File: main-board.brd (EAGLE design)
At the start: 49.2 x 17.8 mm, 53 parts, among them IC1 MEGA328-PB, IC2 MCP73831, IC3 LE33, Q1 3,6864 MHz, Q4 TSM2302CX, T1 IRF7306

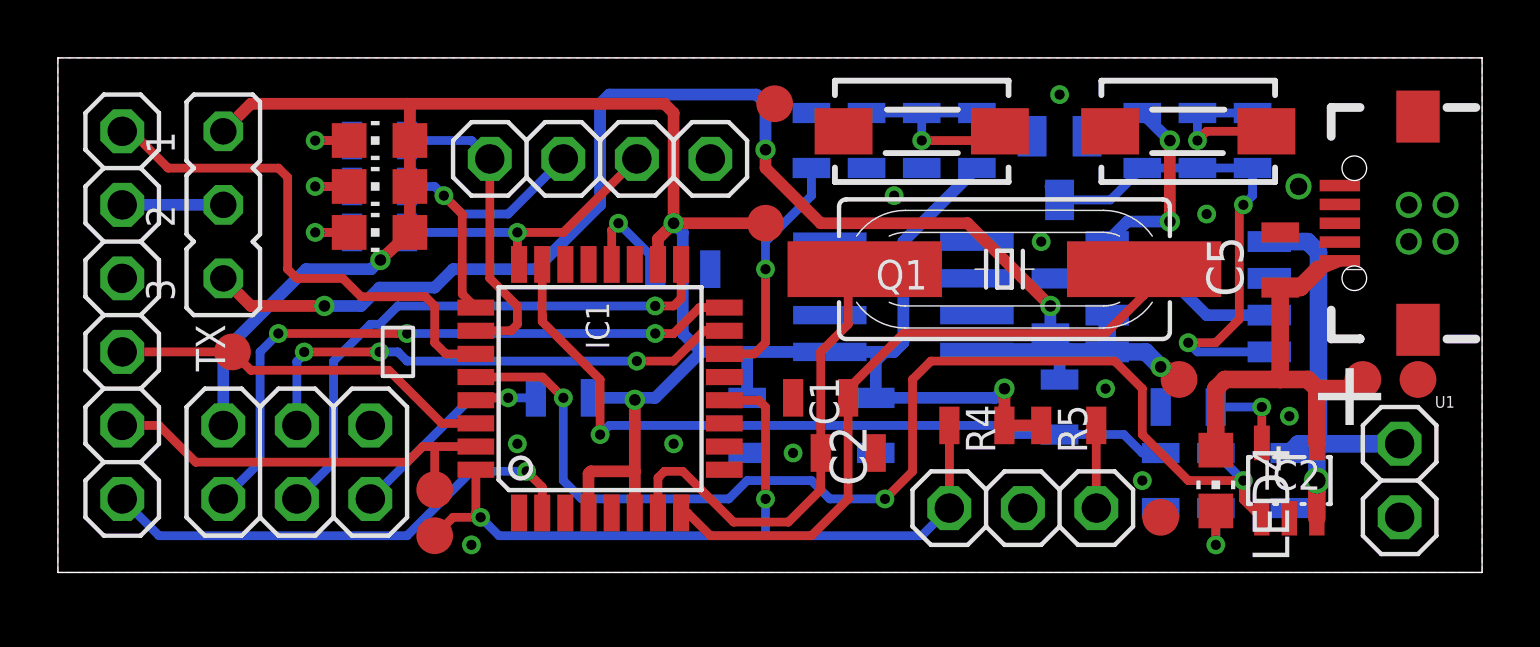
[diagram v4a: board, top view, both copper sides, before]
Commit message: Fix polarity-protection MOSFET.
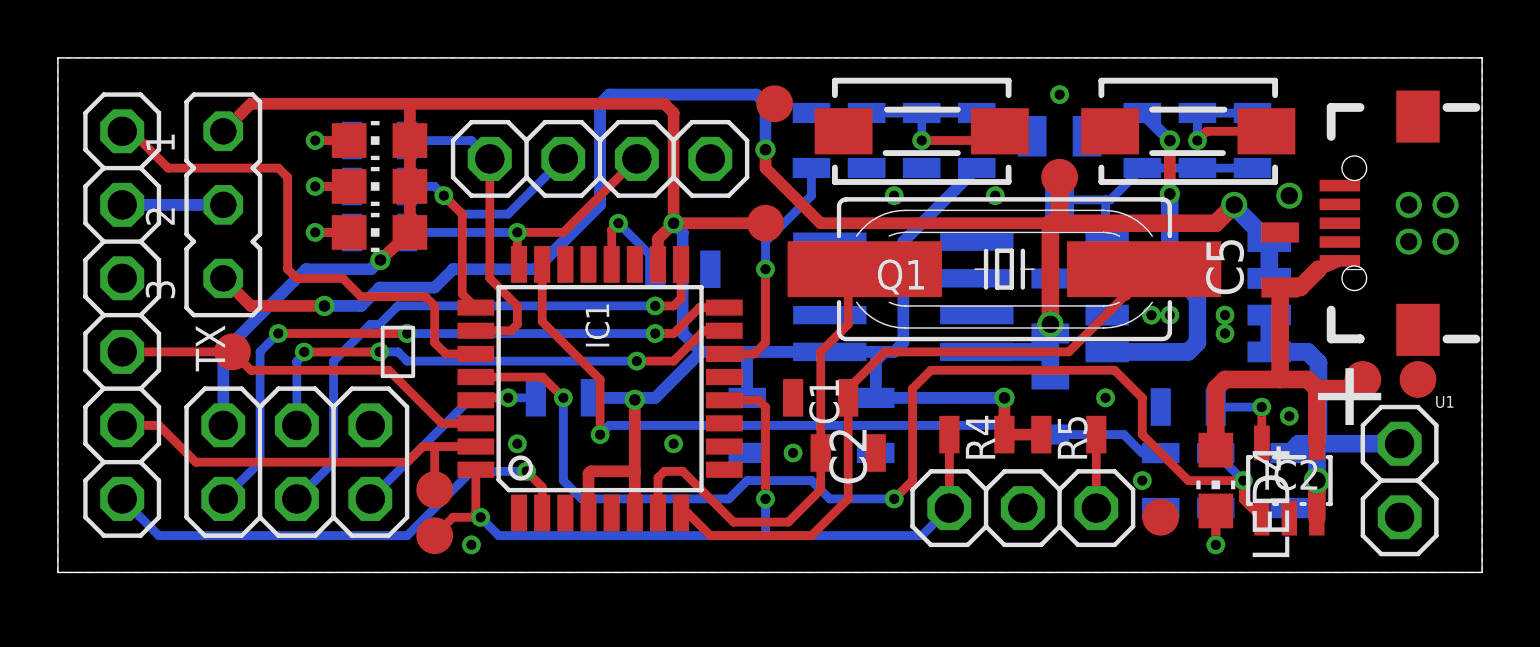
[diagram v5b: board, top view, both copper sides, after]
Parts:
- moved TP5 8.11 mm to (34.6, 13.7)
- moved R7 0.32 mm to (34.3, 5.71)
- moved R4 0.32 mm to (31.8, 4.76)
- moved R5 0.32 mm to (34.9, 4.76)
- turned T1 to 90 degrees
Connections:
- net BAT-POS-VCC: now also T1.1; no longer T1.7, T1.8
- net BAT-RAW-VCC: now also T1.7, T1.8; no longer T1.1
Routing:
- net START_GATE: track 18.1 -> 9.15 mm, vias 2 -> 0
- net VCC-BAT: track 49.8 -> 56.4 mm
- net BAT-RAW-VCC: track 15.0 -> 12.5 mm

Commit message: Add diode to CHARGE-STAT pin.
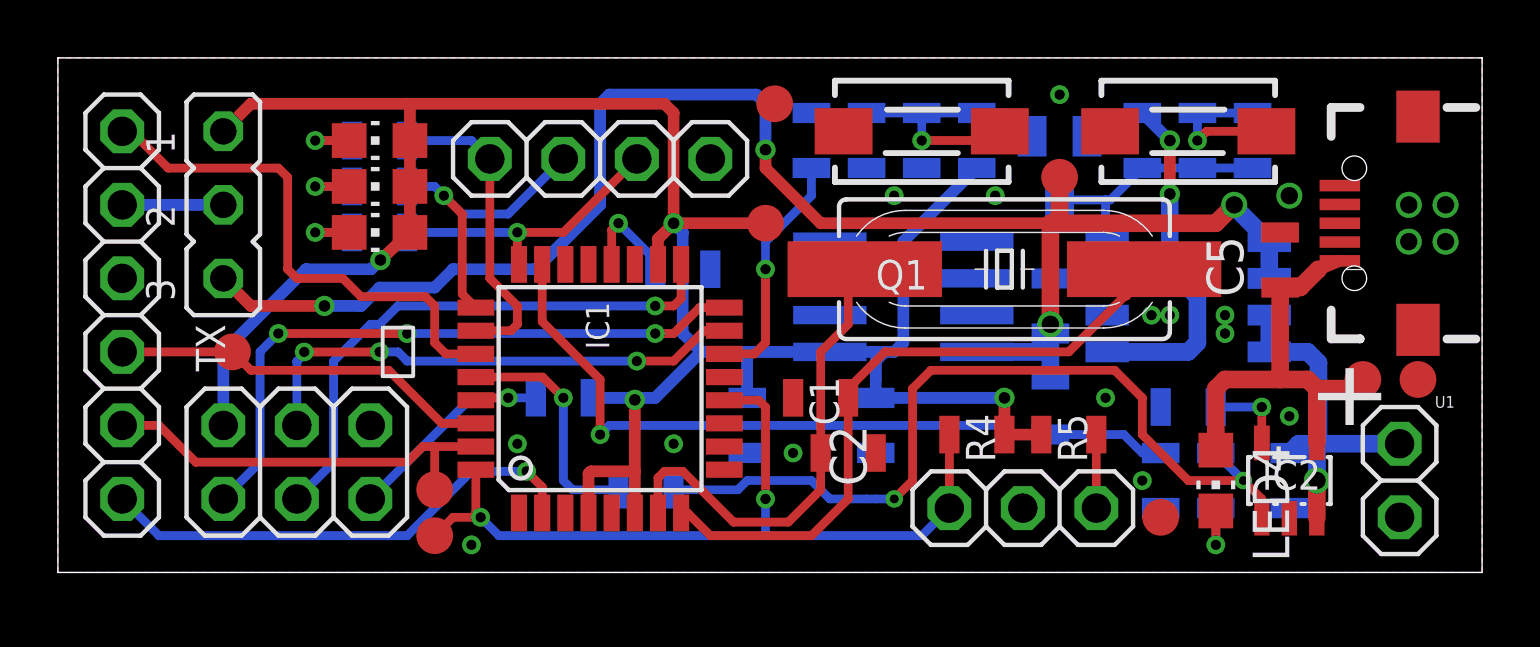
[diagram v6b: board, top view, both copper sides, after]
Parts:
- added D1: 1N4148-0805, diode:R0805
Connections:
- new net CHARGE-STAT-INT: D1.K, IC2.1, R14.1
- net CHARGE-STAT: now also D1.A; no longer IC2.1, R14.1
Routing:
- net CHARGE-STAT: track 39.4 -> 8.22 mm, vias 3 -> 1
- net CHARGE-STAT-INT: track 0.00 -> 29.0 mm, vias 0 -> 2
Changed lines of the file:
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@@
 <grid distance="1.27" unitdist="mm" unit="mm" style="dots" multiple="2" display="no" altdistance="0.3175" altunitdist="mm" altunit="mm"/>
 <layers>
-<layer number="1" name="Top" color="3" fill="1" visible="yes" active="yes"/>
+<layer number="1" name="Top" color="3" fill="1" visible="no" active="yes"/>
 <layer number="2" name="Route2" color="1" fill="3" visible="no" active="no"/>
 <layer number="3" name="Route3" color="4" fill="3" visible="no" active="no"/>
@@
 <layer number="19" name="Unrouted" color="6" fill="1" visible="yes" active="yes"/>
 <layer number="20" name="Dimension" color="24" fill="1" visible="yes" active="yes"/>
-<layer number="21" name="tPlace" color="7" fill="1" visible="yes" active="yes"/>
+<layer number="21" name="tPlace" color="7" fill="1" visible="no" active="yes"/>
 <layer number="22" name="bPlace" color="7" fill="1" visible="yes" active="yes"/>
-<layer number="23" name="tOrigins" color="15" fill="1" visible="yes" active="yes"/>
+<layer number="23" name="tOrigins" color="15" fill="1" visible="no" active="yes"/>
 <layer number="24" name="bOrigins" color="15" fill="1" visible="yes" active="yes"/>
 <layer number="25" name="tNames" color="7" fill="1" visible="no" active="yes"/>
@@
 <layer number="44" name="Drills" color="7" fill="1" visible="no" active="yes"/>
 <layer number="45" name="Holes" color="7" fill="1" visible="no" active="yes"/>
-<layer number="46" name="Milling" color="3" fill="1" visible="yes" active="yes"/>
+<layer number="46" name="Milling" color="3" fill="1" visible="no" active="yes"/>
 <layer number="47" name="Measures" color="7" fill="1" visible="no" active="yes"/>
 <layer number="48" name="Document" color="7" fill="1" visible="no" active="yes"/>
-<layer number="49" name="Reference" color="7" fill="1" visible="yes" active="yes"/>
+<layer number="49" name="Reference" color="7" fill="1" visible="no" active="yes"/>
 <layer number="50" name="dxf" color="7" fill="1" visible="no" active="no"/>
-<layer number="51" name="tDocu" color="7" fill="1" visible="yes" active="yes"/>
+<layer number="51" name="tDocu" color="7" fill="1" visible="no" active="yes"/>
 <layer number="52" name="bDocu" color="7" fill="1" visible="yes" active="yes"/>
 <layer number="53" name="tGND_GNDA" color="7" fill="9" visible="no" active="no"/>
@@
 <attribute name="VALUE" x="32.385" y="19.05" size="1.27" layer="27" rot="R180"/>
 </element>
+<element name="D1" library="diode" package="R0805" value="1N4148-0805" x="20.32" y="2.8575" rot="MR180"/>
 </elements>
 <signals>
@@
 </signal>
 <signal name="CHARGE-STAT">
-<contactref element="IC2" pad="1"/>
-<contactref element="R14" pad="1"/>
-<via x="40.9575" y="3.175" extent="1-16" drill="0.35"/>
-<wire x1="40.9575" y1="3.175" x2="39.0525" y2="3.175" width="0.3048" layer="1"/>
-<wire x1="39.0525" y1="3.175" x2="37.465" y2="4.7625" width="0.3048" layer="1"/>
-<wire x1="37.465" y1="6.0325" x2="36.5125" y2="6.985" width="0.3048" layer="1"/>
-<wire x1="36.5125" y1="6.985" x2="30.1625" y2="6.985" width="0.3048" layer="1"/>
-<wire x1="37.465" y1="4.7625" x2="37.465" y2="6.0325" width="0.3048" layer="1"/>
-<wire x1="30.1625" y1="6.985" x2="29.5275" y2="6.35" width="0.3048" layer="1"/>
-<wire x1="29.5275" y1="6.35" x2="29.5275" y2="3.175" width="0.3048" layer="1"/>
-<wire x1="29.5275" y1="3.175" x2="28.8925" y2="2.54" width="0.3048" layer="1"/>
-<via x="28.8925" y="2.54" extent="1-16" drill="0.35"/>
-<wire x1="18.0975" y1="2.54" x2="17.4625" y2="3.175" width="0.3048" layer="16"/>
 <wire x1="17.4625" y1="3.175" x2="17.4625" y2="6.0325" width="0.3048" layer="16"/>
 <via x="17.4625" y="6.0325" extent="1-16" drill="0.35"/>
-<wire x1="40.9575" y1="3.175" x2="40.0075" y2="4.125" width="0.3048" layer="16"/>
-<wire x1="40.0075" y1="4.125" x2="40.005" y2="4.125" width="0.3048" layer="16"/>
-<wire x1="40.9575" y1="3.175" x2="40.9575" y2="2.5125" width="0.3048" layer="1"/>
-<wire x1="40.9575" y1="2.5125" x2="41.595" y2="1.875" width="0.3048" layer="1"/>
-<wire x1="28.8925" y1="2.54" x2="26.67" y2="2.54" width="0.3048" layer="16"/>
-<wire x1="26.67" y1="2.54" x2="26.035" y2="3.175" width="0.3048" layer="16"/>
-<wire x1="26.035" y1="3.175" x2="23.8125" y2="3.175" width="0.3048" layer="16"/>
-<wire x1="23.8125" y1="3.175" x2="23.1775" y2="2.54" width="0.3048" layer="16"/>
-<wire x1="23.1775" y1="2.54" x2="18.0975" y2="2.54" width="0.3048" layer="16"/>
 <contactref element="IC1" pad="28"/>
 <wire x1="14.4399" y1="6.75" x2="16.745" y2="6.75" width="0.3048" layer="1"/>
 <wire x1="16.745" y1="6.75" x2="17.4625" y2="6.0325" width="0.3048" layer="1"/>
+<contactref element="D1" pad="A"/>
+<wire x1="19.37" y1="2.8575" x2="17.78" y2="2.8575" width="0.3" layer="16"/>
+<wire x1="17.78" y1="2.8575" x2="17.4625" y2="3.175" width="0.3" layer="16"/>
 </signal>
 <signal name="CHARGE-STAT-LED">
@@
 <wire x1="38.4175" y1="13.075" x2="38.4175" y2="10.16" width="0.6096" layer="16"/>
 </signal>
+<signal name="CHARGE-STAT-INT">
+<contactref element="IC2" pad="1"/>
+<contactref element="R14" pad="1"/>
+<contactref element="D1" pad="K"/>
+<wire x1="21.27" y1="2.8575" x2="23.495" y2="2.8575" width="0.3" layer="16"/>
+<wire x1="23.495" y1="2.8575" x2="23.8125" y2="3.175" width="0.3" layer="16"/>
+<wire x1="26.035" y1="3.175" x2="26.67" y2="2.54" width="0.3" layer="16"/>
+<wire x1="26.67" y1="2.54" x2="27.94" y2="2.54" width="0.3" layer="16"/>
+<wire x1="27.94" y1="2.54" x2="28.2575" y2="2.54" width="0.3" layer="16"/>
+<wire x1="23.8125" y1="3.175" x2="26.035" y2="3.175" width="0.3" layer="16"/>
+<wire x1="29.5275" y1="6.35" x2="29.5275" y2="3.175" width="0.3048" layer="1"/>
+<wire x1="29.5275" y1="6.35" x2="30.1625" y2="6.985" width="0.3048" layer="1"/>
+<wire x1="30.1625" y1="6.985" x2="36.5125" y2="6.985" width="0.3048" layer="1"/>
+<wire x1="36.5125" y1="6.985" x2="37.465" y2="6.0325" width="0.3048" layer="1"/>
+<wire x1="37.465" y1="6.0325" x2="37.465" y2="4.7625" width="0.3048" layer="1"/>
+<wire x1="37.465" y1="4.7625" x2="39.0525" y2="3.175" width="0.3048" layer="1"/>
+<wire x1="39.0525" y1="3.175" x2="40.3225" y2="3.175" width="0.3048" layer="1"/>
+<via x="40.9575" y="3.175" extent="1-16" drill="0.3048"/>
+<wire x1="40.3225" y1="3.175" x2="40.9575" y2="3.175" width="0.3" layer="1"/>
+<wire x1="40.005" y1="4.125" x2="40.0075" y2="4.125" width="0.3" layer="16"/>
+<wire x1="40.0075" y1="4.125" x2="40.9575" y2="3.175" width="0.3" layer="16"/>
+<wire x1="41.595" y1="1.875" x2="41.595" y2="2.5375" width="0.3" layer="1"/>
+<wire x1="41.595" y1="2.5375" x2="40.9575" y2="3.175" width="0.3" layer="1"/>
+<via x="28.8925" y="2.54" extent="1-16" drill="0.3048"/>
+<wire x1="29.5275" y1="3.175" x2="28.8925" y2="2.54" width="0.3" layer="1"/>
+<wire x1="28.2575" y1="2.54" x2="28.8925" y2="2.54" width="0.3" layer="16"/>
+</signal>
 </signals>

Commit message: Change value of C9.
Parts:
- C9: value 10u -> 100n
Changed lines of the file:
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@@
 <attribute name="VALUE" x="38.735" y="13.6525" size="1.27" layer="28" rot="MR90"/>
 </element>
-<element name="C9" library="rcl" package="C0805" value="10u" x="27.94" y="14.9225" smashed="yes" rot="MR270">
+<element name="C9" library="rcl" package="C0805" value="100n" x="27.94" y="14.9225" smashed="yes" rot="MR270">
 <attribute name="NAME" x="26.9875" y="13.335" size="1.016" layer="26" rot="MR180"/>
 <attribute name="VALUE" x="30.48" y="16.1925" size="1.27" layer="28" rot="MR270"/>

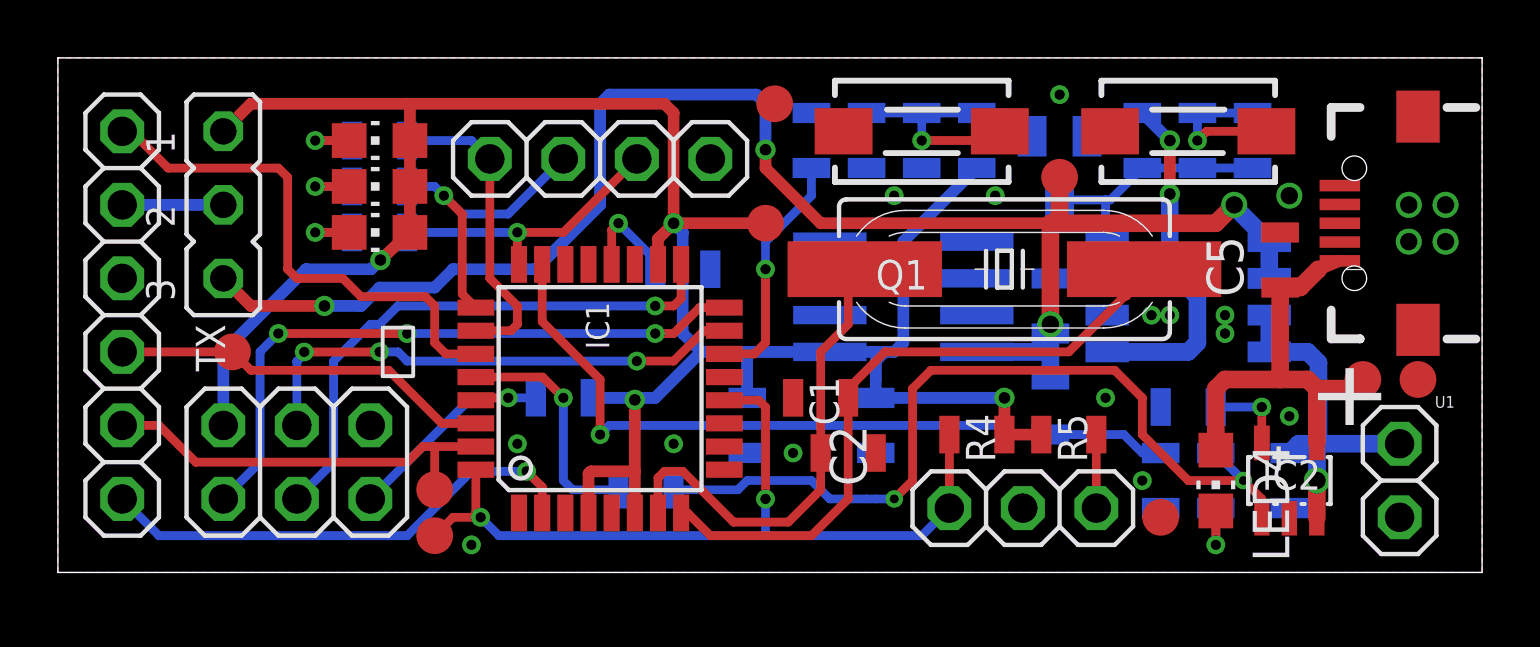
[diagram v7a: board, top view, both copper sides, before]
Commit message: Use SJ2W for BT power switching.
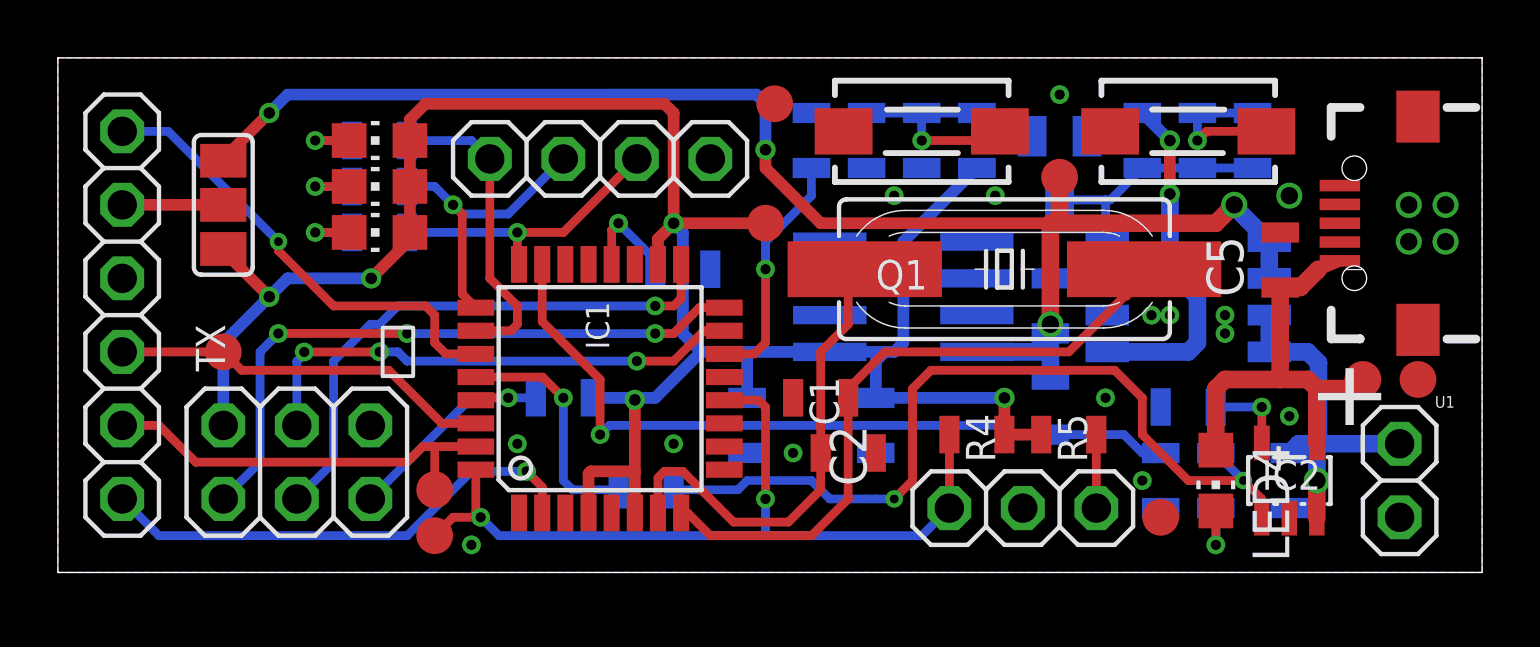
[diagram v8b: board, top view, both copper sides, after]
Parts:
- JP-BT-POWER: value PINHEAD -> (none); device jumper:JP2 -> jumper:SJ_2
- moved TP8 0.32 mm to (5.71, 7.62)
- turned JP-BT-POWER to 90 degrees
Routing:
- net VCC-BAT: track 56.4 -> 51.9 mm
- net VCC: track 80.7 -> 76.3 mm, vias 4 -> 5
- net BT-EN: track 18.0 -> 16.1 mm, vias 0 -> 1
